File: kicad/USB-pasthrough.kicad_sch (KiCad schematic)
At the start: 93 parts, among them J1 USB_Power, J2 USB_C, J3 Cortex Debug, J4 Power_Sel, J5 SPI Display, J6 SWD, J7 USB_A, J8 MicroSD, SW1 Boot0, SW2 Reset, U1 AMS1117, U2 STM32F723VET6, Y1 8 MHz

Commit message: Change incorrect metric footprints to imperial
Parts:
- R18, R19, R20, R21, R22, R23: footprint Resistor_SMD:R_0201_0603Metric_Pad0.64x0.40mm_HandSolder -> Resistor_SMD:R_0603_1608Metric_Pad0.98x0.95mm_HandSolder
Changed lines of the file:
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@@
     (property "Reference" "R18" (id 0) (at 34.29 115.57 90))
     (property "Value" "33" (id 1) (at 39.37 118.11 90))
-    (property "Footprint" "Resistor_SMD:R_0201_0603Metric_Pad0.64x0.40mm_HandSolder" (id 2) (at 36.83 116.84 0)
+    (property "Footprint" "Resistor_SMD:R_0603_1608Metric_Pad0.98x0.95mm_HandSolder" (id 2) (at 36.83 116.84 0)
       (effects (font (size 1.27 1.27)) hide)
     )
@@
     (property "Reference" "R21" (id 0) (at 247.65 81.28 90))
     (property "Value" "68" (id 1) (at 247.65 83.82 90))
-    (property "Footprint" "Resistor_SMD:R_0201_0603Metric_Pad0.64x0.40mm_HandSolder" (id 2) (at 247.65 87.63 0)
+    (property "Footprint" "Resistor_SMD:R_0603_1608Metric_Pad0.98x0.95mm_HandSolder" (id 2) (at 247.65 87.63 0)
       (effects (font (size 1.27 1.27)) hide)
     )
@@
     (property "Reference" "R19" (id 0) (at 34.29 105.41 90))
     (property "Value" "150" (id 1) (at 40.64 107.95 90))
-    (property "Footprint" "Resistor_SMD:R_0201_0603Metric_Pad0.64x0.40mm_HandSolder" (id 2) (at 36.83 106.68 0)
+    (property "Footprint" "Resistor_SMD:R_0603_1608Metric_Pad0.98x0.95mm_HandSolder" (id 2) (at 36.83 106.68 0)
       (effects (font (size 1.27 1.27)) hide)
     )
@@
     (property "Reference" "R22" (id 0) (at 248.92 115.57 90))
     (property "Value" "150" (id 1) (at 248.92 118.11 90))
-    (property "Footprint" "Resistor_SMD:R_0201_0603Metric_Pad0.64x0.40mm_HandSolder" (id 2) (at 248.92 121.92 0)
+    (property "Footprint" "Resistor_SMD:R_0603_1608Metric_Pad0.98x0.95mm_HandSolder" (id 2) (at 248.92 121.92 0)
       (effects (font (size 1.27 1.27)) hide)
     )
@@
     (property "Reference" "R20" (id 0) (at 34.29 110.49 90))
     (property "Value" "68" (id 1) (at 39.37 113.03 90))
-    (property "Footprint" "Resistor_SMD:R_0201_0603Metric_Pad0.64x0.40mm_HandSolder" (id 2) (at 36.83 111.76 0)
+    (property "Footprint" "Resistor_SMD:R_0603_1608Metric_Pad0.98x0.95mm_HandSolder" (id 2) (at 36.83 111.76 0)
       (effects (font (size 1.27 1.27)) hide)
     )
@@
     (property "Reference" "R23" (id 0) (at 194.31 16.51 90))
     (property "Value" "33" (id 1) (at 194.31 19.05 90))
-    (property "Footprint" "Resistor_SMD:R_0201_0603Metric_Pad0.64x0.40mm_HandSolder" (id 2) (at 194.31 22.86 0)
+    (property "Footprint" "Resistor_SMD:R_0603_1608Metric_Pad0.98x0.95mm_HandSolder" (id 2) (at 194.31 22.86 0)
       (effects (font (size 1.27 1.27)) hide)
     )
@@
     )
     (path "/10047197-f37d-4252-88d5-541fa667cf49"
-      (reference "R18") (unit 1) (value "33") (footprint "Resistor_SMD:R_0201_0603Metric_Pad0.64x0.40mm_HandSolder")
+      (reference "R18") (unit 1) (value "33") (footprint "Resistor_SMD:R_0603_1608Metric_Pad0.98x0.95mm_HandSolder")
     )
     (path "/688c83a9-d3a0-48bd-9a79-8cb908305852"
-      (reference "R19") (unit 1) (value "150") (footprint "Resistor_SMD:R_0201_0603Metric_Pad0.64x0.40mm_HandSolder")
+      (reference "R19") (unit 1) (value "150") (footprint "Resistor_SMD:R_0603_1608Metric_Pad0.98x0.95mm_HandSolder")
     )
     (path "/c140c3a9-ace7-4aca-a1de-aa6064cf6484"
-      (reference "R20") (unit 1) (value "68") (footprint "Resistor_SMD:R_0201_0603Metric_Pad0.64x0.40mm_HandSolder")
+      (reference "R20") (unit 1) (value "68") (footprint "Resistor_SMD:R_0603_1608Metric_Pad0.98x0.95mm_HandSolder")
     )
     (path "/1a82aba1-7bcd-415b-b242-a8697f42897d"
-      (reference "R21") (unit 1) (value "68") (footprint "Resistor_SMD:R_0201_0603Metric_Pad0.64x0.40mm_HandSolder")
+      (reference "R21") (unit 1) (value "68") (footprint "Resistor_SMD:R_0603_1608Metric_Pad0.98x0.95mm_HandSolder")
     )
     (path "/6e07490e-b1ba-4686-bc5c-17b021c96957"
-      (reference "R22") (unit 1) (value "150") (footprint "Resistor_SMD:R_0201_0603Metric_Pad0.64x0.40mm_HandSolder")
+      (reference "R22") (unit 1) (value "150") (footprint "Resistor_SMD:R_0603_1608Metric_Pad0.98x0.95mm_HandSolder")
     )
     (path "/d4e6855f-877c-4251-bf9e-698081c7e725"
-      (reference "R23") (unit 1) (value "33") (footprint "Resistor_SMD:R_0201_0603Metric_Pad0.64x0.40mm_HandSolder")
+      (reference "R23") (unit 1) (value "33") (footprint "Resistor_SMD:R_0603_1608Metric_Pad0.98x0.95mm_HandSolder")
     )
     (path "/7fb86b33-f6c8-4735-8ebb-bbd50db9e462"

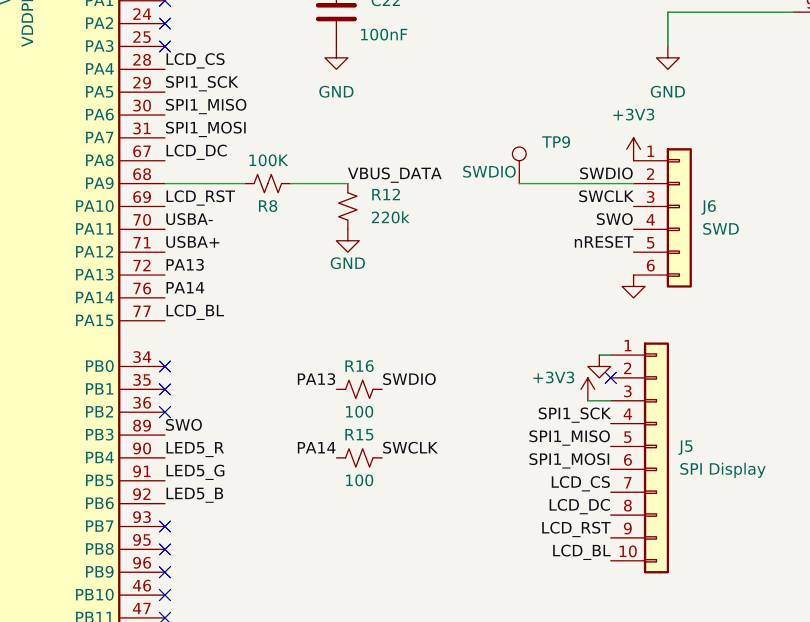
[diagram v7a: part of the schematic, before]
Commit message: Clean up SWD connector
Make pins conform to Nucleo connector
Rename SoC to R signals
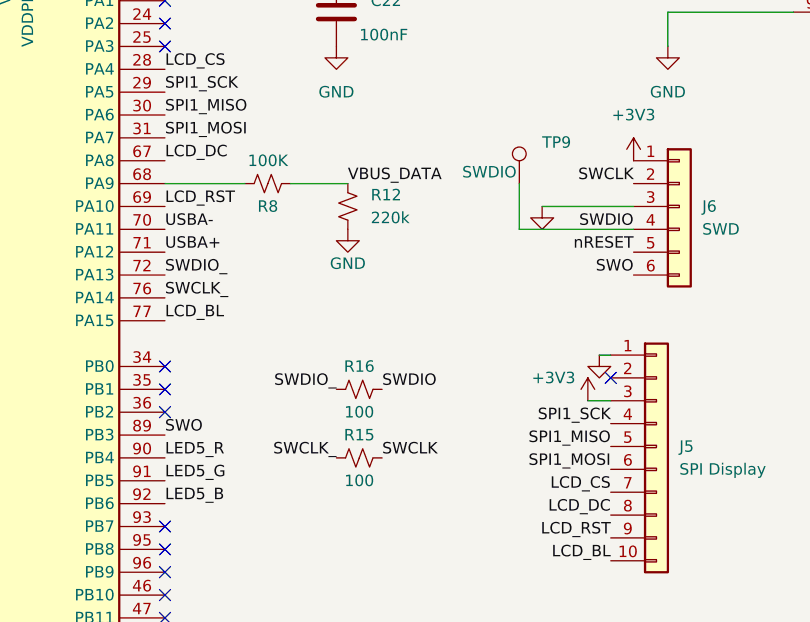
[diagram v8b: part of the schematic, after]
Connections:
- net GND: now also J6.3 (Pin_3); no longer J6.6 (Pin_6)
- net SWCLK: now also J6.2 (Pin_2); no longer J6.3 (Pin_3)
- net SWDIO: now also J6.4 (Pin_4); no longer J6.2 (Pin_2)
- net SWO: now also J6.6 (Pin_6); no longer J6.4 (Pin_4)
- net PA13 renamed SWDIO_
- net PA14 renamed SWCLK_
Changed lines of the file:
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@@
+    (stroke (width 0) (type default) (color 0 0 0 0))
+  )
+  (wire (pts (xy 171.45 88.9) (xy 171.45 83.82))
     (stroke (width 0) (type default) (color 0 0 0 0))
   )
@@
     (stroke (width 0) (type default) (color 0 0 0 0))
   )
+  (wire (pts (xy 184.15 88.9) (xy 171.45 88.9))
+    (stroke (width 0) (type default) (color 0 0 0 0))
+  )
+  (wire (pts (xy 173.99 86.36) (xy 184.15 86.36))
+    (stroke (width 0) (type default) (color 0 0 0 0))
+  )
   (wire (pts (xy 132.08 167.64) (xy 143.51 167.64))
     (stroke (width 0) (type default) (color 0 0 0 0))
@@
     (stroke (width 0) (type default) (color 0 0 0 0))
   )
-  (wire (pts (xy 171.45 83.82) (xy 184.15 83.82))
-    (stroke (width 0) (type default) (color 0 0 0 0))
-  )
   (wire (pts (xy 201.93 64.77) (xy 187.96 64.77))
     (stroke (width 0) (type default) (color 0 0 0 0))
@@
     (effects (font (size 1.27 1.27)) (justify left bottom))
   )
-  (label "SWCLK" (at 184.15 86.36 180)
+  (label "SWCLK" (at 184.15 83.82 180)
     (effects (font (size 1.27 1.27)) (justify right bottom))
   )
@@
     (effects (font (size 1.27 1.27)) (justify right bottom))
   )
-  (label "PA13" (at 151.13 106.68 180)
+  (label "SWDIO_" (at 151.13 106.68 180)
     (effects (font (size 1.27 1.27)) (justify right bottom))
   )
@@
     (effects (font (size 1.27 1.27)) (justify left bottom))
   )
-  (label "PA14" (at 132.08 96.52 0)
+  (label "SWCLK_" (at 132.08 96.52 0)
     (effects (font (size 1.27 1.27)) (justify left bottom))
   )
@@
     (effects (font (size 1.27 1.27)) (justify left bottom))
   )
-  (label "SWO" (at 184.15 88.9 180)
+  (label "SWO" (at 184.15 93.98 180)
     (effects (font (size 1.27 1.27)) (justify right bottom))
   )
@@
     (effects (font (size 1.27 1.27)) (justify right bottom))
   )
-  (label "PA13" (at 132.08 93.98 0)
-    (effects (font (size 1.27 1.27)) (justify left bottom))
-  )
-  (label "SWDIO" (at 184.15 83.82 180)
+  (label "SWDIO_" (at 132.08 93.98 0)
+    (effects (font (size 1.27 1.27)) (justify left bottom))
+  )
+  (label "SWDIO" (at 184.15 88.9 180)
     (effects (font (size 1.27 1.27)) (justify right bottom))
   )
@@
     (effects (font (size 1.27 1.27)) (justify right bottom))
   )
-  (label "PA14" (at 151.13 114.3 180)
+  (label "SWCLK_" (at 151.13 114.3 180)
     (effects (font (size 1.27 1.27)) (justify right bottom))
   )
@@
     (pin "1")
   )
-  (symbol (lib_id "power:GND") (at 184.15 93.98 0) (unit 1)
-    (in_bom yes) (on_board yes) (fields_autoplaced)
-    (property "Reference" "#PWR042" (id 0) (at 184.15 100.33 0)
-      (effects (font (size 1.27 1.27)) hide)
-    )
-    (property "Value" "GND" (id 1) (at 184.15 99.06 0)
-      (effects (font (size 1.27 1.27)) hide)
-    )
-    (property "Footprint" "" (id 2) (at 184.15 93.98 0)
-      (effects (font (size 1.27 1.27)) hide)
-    )
-    (property "Datasheet" "" (id 3) (at 184.15 93.98 0)
-      (effects (font (size 1.27 1.27)) hide)
-    )
+  (symbol (lib_id "power:GND") (at 173.99 86.36 0) (unit 1)
+    (in_bom yes) (on_board yes) (fields_autoplaced)
+    (property "Reference" "#PWR042" (id 0) (at 173.99 92.71 0)
+      (effects (font (size 1.27 1.27)) hide)
+    )
+    (property "Value" "GND" (id 1) (at 173.99 91.44 0)
+      (effects (font (size 1.27 1.27)) hide)
+    )
+    (property "Footprint" "" (id 2) (at 173.99 86.36 0)
+      (effects (font (size 1.27 1.27)) hide)
+    )
+    (property "Datasheet" "" (id 3) (at 173.99 86.36 0)
+      (effects (font (size 1.27 1.27)) hide)
+    )
